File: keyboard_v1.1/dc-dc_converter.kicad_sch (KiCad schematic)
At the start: 14 parts, among them Q1 AO3400A, U2 max1771esa+T

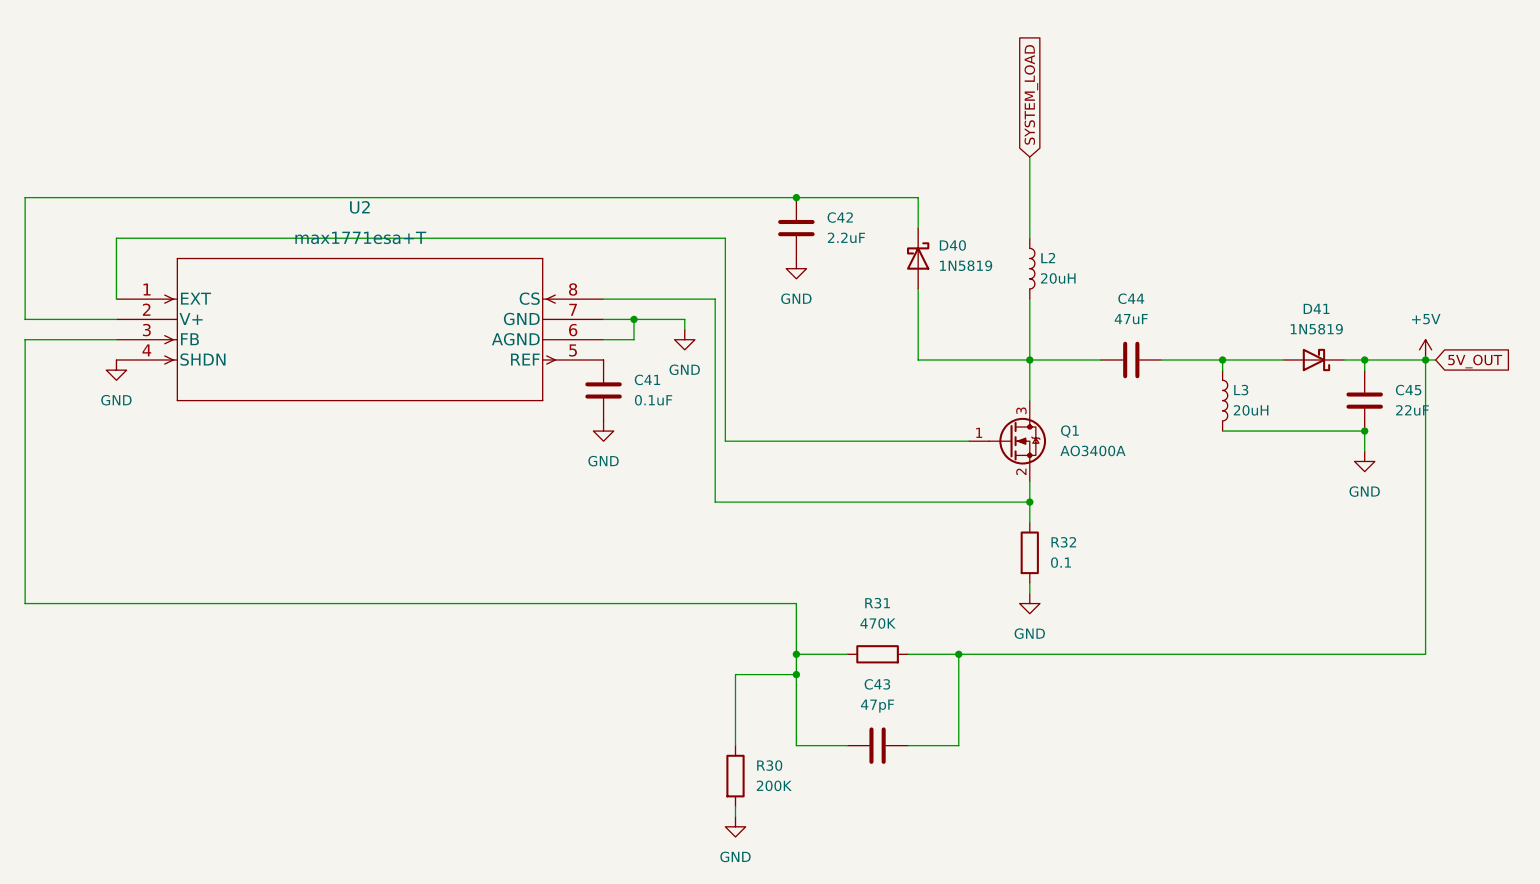
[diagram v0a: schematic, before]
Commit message: New design - schematics added (2022.07.20.)
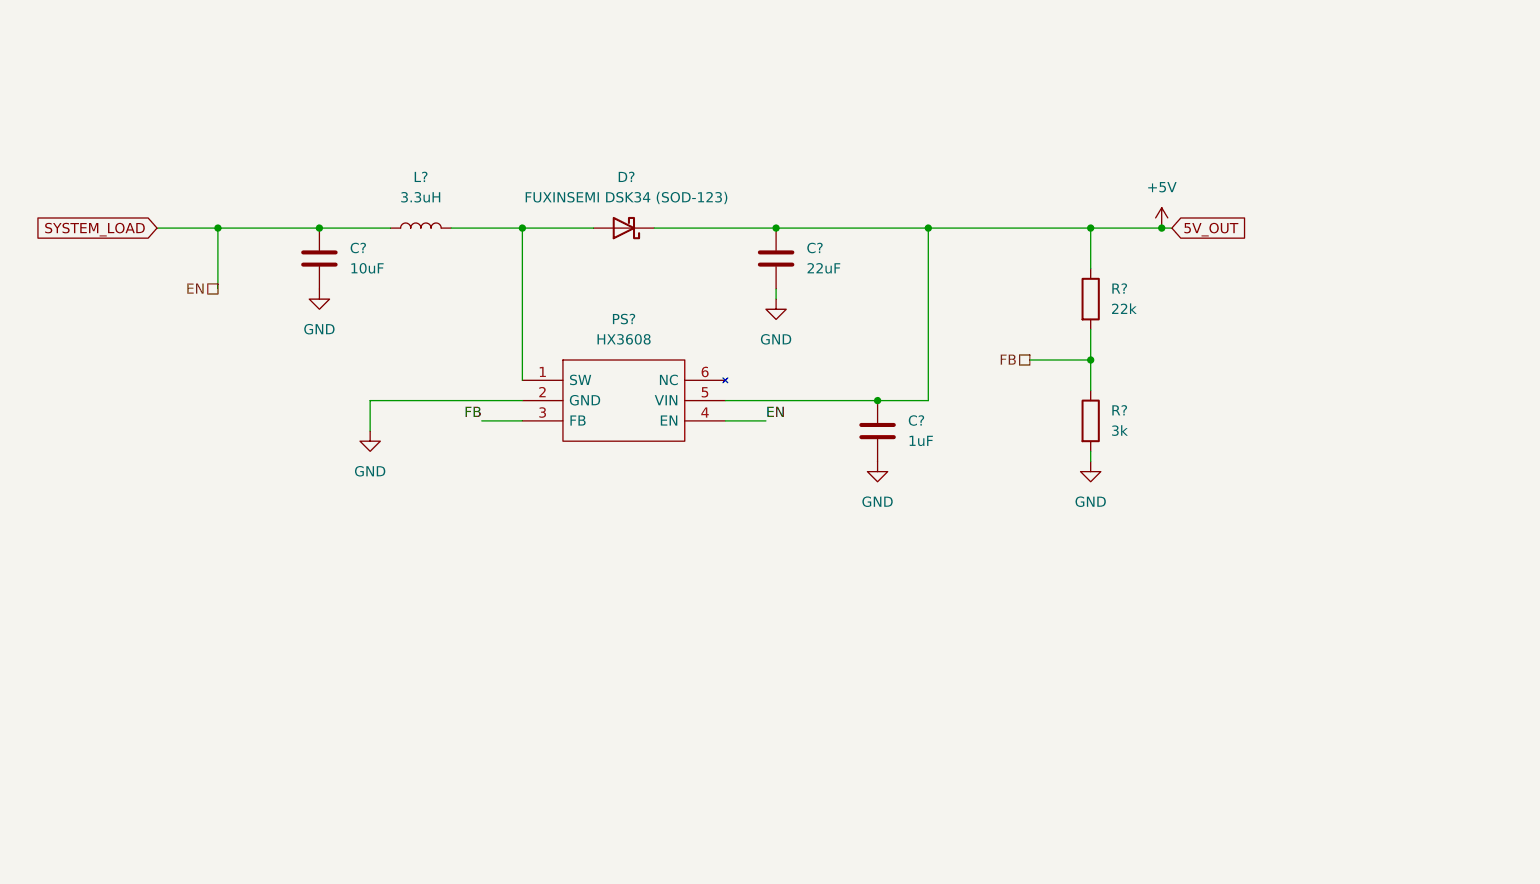
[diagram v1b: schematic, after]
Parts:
- removed C41: 0.1uF, Capacitor_SMD:C_0805_2012Metric_Pad1.18x1.45mm_HandSolder, symbol Device:C
- removed C42: 2.2uF, Capacitor_SMD:C_0805_2012Metric_Pad1.18x1.45mm_HandSolder, symbol Device:C
- removed C43: 47pF, Capacitor_SMD:C_0805_2012Metric_Pad1.18x1.45mm_HandSolder, symbol Device:C
- removed C44: 47uF, Capacitor_THT:CP_Radial_D4.0mm_P1.50mm, symbol Device:C
- removed C45: 22uF, Capacitor_SMD:C_0805_2012Metric_Pad1.18x1.45mm_HandSolder, symbol Device:C
- removed D40, D41: 1N5819, Diode_THT:D_DO-41_SOD81_P10.16mm_Horizontal, symbol Diode:1N5819
- removed L2, L3: 20uH, inductors:inductors, symbol Device:L
- removed Q1: AO3400A, Package_TO_SOT_SMD:SOT-23, symbol Transistor_FET:AO3400A
- removed R30: 200K, Resistor_SMD:R_0805_2012Metric_Pad1.20x1.40mm_HandSolder, symbol Device:R
- removed R31: 470K, Resistor_SMD:R_0805_2012Metric_Pad1.20x1.40mm_HandSolder, symbol Device:R
- removed R32: 0.1, Resistor_SMD:R_0805_2012Metric_Pad1.20x1.40mm_HandSolder, symbol Device:R
- removed U2: max1771esa+T, max1771:max1771esa&plus_T, symbol max1771:max1771esa+T
- added C?: 1uF, Capacitor_SMD:C_0805_2012Metric_Pad1.18x1.45mm_HandSolder, symbol Device:C
- added C?: 10uF, Capacitor_SMD:C_0805_2012Metric_Pad1.18x1.45mm_HandSolder, symbol Device:C
- added C?: 22uF, Capacitor_SMD:C_0805_2012Metric_Pad1.18x1.45mm_HandSolder, symbol Device:C
- added D?: FUXINSEMI DSK34 (SOD-123), Diode_SMD:D_SOD-123, symbol Diode:BAT42W-V
- added L?: 3.3uH, inductors:inductors, symbol Device:L
- added PS?: HX3608, SOT95P280X125-6N, symbol SamacSys_Parts:HX3608
- added R?: 3k, Resistor_SMD:R_0805_2012Metric_Pad1.20x1.40mm_HandSolder, symbol Device:R
- added R?: 22k, Resistor_SMD:R_0805_2012Metric_Pad1.20x1.40mm_HandSolder, symbol Device:R
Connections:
- net +5V: now also C?.1, C?.1, D?.1 (K), PS?.5 (VIN), R?.1
- net GND: now also C?.2, C?.2, C?.2, PS?.2 (GND), R?.2
- net SYSTEM_LOAD: now also C?.1, L?.1, PS?.4 (EN)
- new net: D?.2 (A), L?.2, PS?.1 (SW)
- new net FB: PS?.3 (FB), R?.1, R?.2

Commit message: PCB layout done - 2022.07.25.
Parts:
- L1: renamed from L?; footprint inductors:inductors -> inductors:inductor_koherelec
- PS1: renamed from PS?; footprint SOT95P280X125-6N -> SamacSys_Parts:SOT95P280X125-6N
- gave numbers to parts that had none: 6
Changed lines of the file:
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@@
+    (effects (font (size 1.27 1.27)) (justify left bottom))
+  )
+  (label "FB" (at 171.45 54.61 180)
+    (effects (font (size 1.27 1.27)) (justify right bottom))
+  )
+  (label "EN" (at 69.85 45.72 0)
     (effects (font (size 1.27 1.27)) (justify left bottom))
   )
@@
     )
   )
-  (hierarchical_label "EN" (shape passive) (at 69.85 45.72 180)
-    (effects (font (size 1.27 1.27)) (justify right))
-  )
-  (hierarchical_label "FB" (shape passive) (at 171.45 54.61 180)
-    (effects (font (size 1.27 1.27)) (justify right))
-  )
   (symbol (lib_id "SamacSys_Parts:HX3608") (at 107.95 57.15 0) (unit 1)
     (in_bom yes) (on_board yes) (fields_autoplaced)
-    (property "Reference" "PS?" (id 0) (at 120.65 49.53 0))
+    (property "Reference" "PS1" (id 0) (at 120.65 49.53 0))
     (property "Value" "HX3608" (id 1) (at 120.65 52.07 0))
-    (property "Footprint" "SOT95P280X125-6N" (id 2) (at 129.54 54.61 0)
+    (property "Footprint" "SamacSys_Parts:SOT95P280X125-6N" (id 2) (at 129.54 54.61 0)
       (effects (font (size 1.27 1.27)) (justify left) hide)
     )
@@
   (symbol (lib_id "power:GND") (at 88.9 63.5 0) (unit 1)
     (in_bom yes) (on_board yes) (fields_autoplaced)
-    (property "Reference" "#PWR?" (id 0) (at 88.9 69.85 0)
+    (property "Reference" "#PWR0142" (id 0) (at 88.9 69.85 0)
       (effects (font (size 1.27 1.27)) hide)
     )
@@
   (symbol (lib_id "Device:L") (at 95.25 38.1 90) (unit 1)
     (in_bom yes) (on_board yes) (fields_autoplaced)
-    (property "Reference" "L?" (id 0) (at 95.25 31.75 90))
+    (property "Reference" "L1" (id 0) (at 95.25 31.75 90))
     (property "Value" "3.3uH" (id 1) (at 95.25 34.29 90))
-    (property "Footprint" "inductors:inductors" (id 2) (at 95.25 38.1 0)
+    (property "Footprint" "inductors:inductor_koherelec" (id 2) (at 95.25 38.1 0)
       (effects (font (size 1.27 1.27)) hide)
     )
@@
   (symbol (lib_id "power:GND") (at 139.7 46.99 0) (unit 1)
     (in_bom yes) (on_board yes) (fields_autoplaced)
-    (property "Reference" "#PWR?" (id 0) (at 139.7 53.34 0)
+    (property "Reference" "#PWR0138" (id 0) (at 139.7 53.34 0)
       (effects (font (size 1.27 1.27)) hide)
     )
@@
   (symbol (lib_id "power:GND") (at 152.4 67.31 0) (unit 1)
     (in_bom yes) (on_board yes) (fields_autoplaced)
-    (property "Reference" "#PWR?" (id 0) (at 152.4 73.66 0)
+    (property "Reference" "#PWR0141" (id 0) (at 152.4 73.66 0)
       (effects (font (size 1.27 1.27)) hide)
     )
@@
   (symbol (lib_id "power:GND") (at 179.07 67.31 0) (unit 1)
     (in_bom yes) (on_board yes) (fields_autoplaced)
-    (property "Reference" "#PWR?" (id 0) (at 179.07 73.66 0)
+    (property "Reference" "#PWR0140" (id 0) (at 179.07 73.66 0)
       (effects (font (size 1.27 1.27)) hide)
     )
@@
   (symbol (lib_id "Device:C") (at 152.4 63.5 0) (unit 1)
     (in_bom yes) (on_board yes) (fields_autoplaced)
-    (property "Reference" "C?" (id 0) (at 156.21 62.2299 0)
+    (property "Reference" "C16" (id 0) (at 156.21 62.2299 0)
       (effects (font (size 1.27 1.27)) (justify left))
     )
@@
   (symbol (lib_id "Device:R") (at 179.07 62.23 0) (unit 1)
     (in_bom yes) (on_board yes) (fields_autoplaced)
-    (property "Reference" "R?" (id 0) (at 181.61 60.9599 0)
+    (property "Reference" "R16" (id 0) (at 181.61 60.9599 0)
       (effects (font (size 1.27 1.27)) (justify left))
     )
@@
   (symbol (lib_id "Diode:BAT42W-V") (at 120.65 38.1 180) (unit 1)
     (in_bom yes) (on_board yes) (fields_autoplaced)
-    (property "Reference" "D?" (id 0) (at 120.9675 31.75 0))
+    (property "Reference" "D13" (id 0) (at 120.9675 31.75 0))
     (property "Value" "FUXINSEMI DSK34 (SOD-123)" (id 1) (at 120.9675 34.29 0))
     (property "Footprint" "Diode_SMD:D_SOD-123" (id 2) (at 120.65 33.655 0)
@@
   (symbol (lib_id "Device:C") (at 82.55 41.91 0) (unit 1)
     (in_bom yes) (on_board yes) (fields_autoplaced)
-    (property "Reference" "C?" (id 0) (at 86.36 40.6399 0)
+    (property "Reference" "C13" (id 0) (at 86.36 40.6399 0)
       (effects (font (size 1.27 1.27)) (justify left))
     )
@@
   (symbol (lib_id "power:GND") (at 82.55 45.72 0) (unit 1)
     (in_bom yes) (on_board yes) (fields_autoplaced)
-    (property "Reference" "#PWR?" (id 0) (at 82.55 52.07 0)
+    (property "Reference" "#PWR0143" (id 0) (at 82.55 52.07 0)
       (effects (font (size 1.27 1.27)) hide)
     )
@@
   (symbol (lib_id "power:+5V") (at 187.96 38.1 0) (unit 1)
     (in_bom yes) (on_board yes) (fields_autoplaced)
-    (property "Reference" "#PWR?" (id 0) (at 187.96 41.91 0)
+    (property "Reference" "#PWR0139" (id 0) (at 187.96 41.91 0)
       (effects (font (size 1.27 1.27)) hide)
     )
@@
   (symbol (lib_id "Device:R") (at 179.07 46.99 0) (unit 1)
     (in_bom yes) (on_board yes) (fields_autoplaced)
-    (property "Reference" "R?" (id 0) (at 181.61 45.7199 0)
+    (property "Reference" "R15" (id 0) (at 181.61 45.7199 0)
       (effects (font (size 1.27 1.27)) (justify left))
     )
@@
   (symbol (lib_id "Device:C") (at 139.7 41.91 0) (unit 1)
     (in_bom yes) (on_board yes) (fields_autoplaced)
-    (property "Reference" "C?" (id 0) (at 143.51 40.6399 0)
-      (effects (font (size 1.27 1.27)) (justify left))
-    )
+    (property "Reference" "C15" (id 0) (at 143.51 40.6399 0)
+      (effects (font (size 1.27 1.27)) (justify left))
+    )
